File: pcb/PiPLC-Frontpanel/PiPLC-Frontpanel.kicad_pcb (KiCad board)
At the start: 2 copper layers, 160 x 43 mm, 3 parts

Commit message: [Frontpanel] Beautify
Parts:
- added REF**: Drill_LED5mm, MeineBib:Drill_LED5mm, F.Cu at (173.2, 103.8)
- added REF**: Drill_LED5mm, MeineBib:Drill_LED5mm, F.Cu at (189.2, 70.8)
- added REF**: Drill_LED5mm, MeineBib:Drill_LED5mm, F.Cu at (197.2, 103.8)
- added REF**: Drill_LED5mm, MeineBib:Drill_LED5mm, F.Cu at (189.2, 103.8)
- added REF**: Drill_LED5mm, MeineBib:Drill_LED5mm, F.Cu at (165.2, 70.8)
- added REF**: Drill_LED5mm, MeineBib:Drill_LED5mm, F.Cu at (157.2, 70.8)
- added REF**: Drill_LED5mm, MeineBib:Drill_LED5mm, F.Cu at (205.2, 103.8)
- added REF**: Drill_LED5mm, MeineBib:Drill_LED5mm, F.Cu at (132.6, 82.3)
- added REF**: Drill_LED5mm, MeineBib:Drill_LED5mm, F.Cu at (149.2, 70.8)
- added REF**: Drill_LED5mm, MeineBib:Drill_LED5mm, F.Cu at (181.2, 103.8)
- added REF**: Drill_LED5mm, MeineBib:Drill_LED5mm, F.Cu at (205.2, 70.8)
- added REF**: Drill_LED5mm, MeineBib:Drill_LED5mm, F.Cu at (149.2, 103.8)
- added REF**: Drill_LED5mm, MeineBib:Drill_LED5mm, F.Cu at (181.2, 70.8)
- added REF**: Drill_LED5mm, MeineBib:Drill_LED5mm, F.Cu at (173.2, 70.8)
- added REF**: Drill_LED5mm, MeineBib:Drill_LED5mm, F.Cu at (132.6, 92.3)
- added REF**: Drill_LED5mm, MeineBib:Drill_LED5mm, F.Cu at (157.2, 103.8)
- added REF**: Drill_LED5mm, MeineBib:Drill_LED5mm, F.Cu at (197.2, 70.8)
- added REF**: Drill_LED5mm, MeineBib:Drill_LED5mm, F.Cu at (165.2, 103.8)
- moved REF** 2.45 mm to (93.4, 94.5)
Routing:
- net (no net): track 0.00 -> 96.8 mm
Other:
- outline, holes or cut-outs redrawn
- board text added: "16A/250V AC | 16A/24V DC Relay outputs"
- board text added: "5-24V active HIGH Optocoupled inputs"

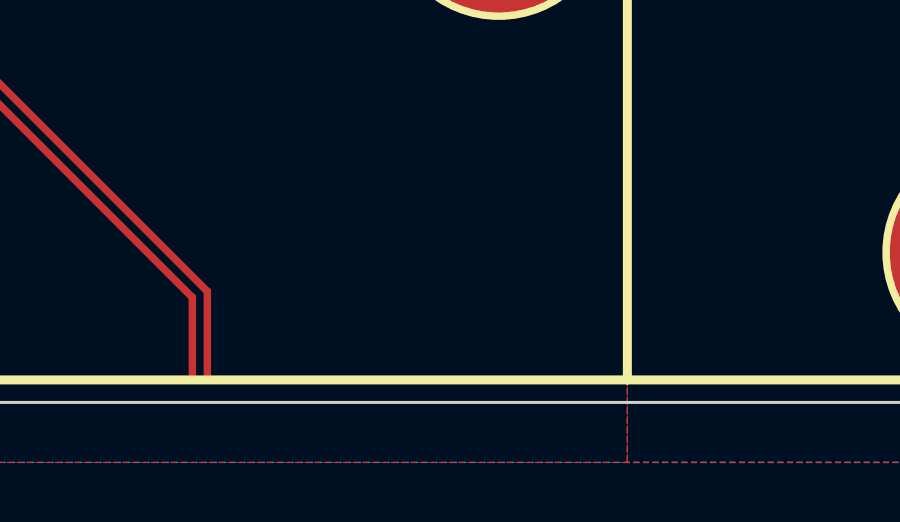
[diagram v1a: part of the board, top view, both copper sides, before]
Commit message: [HMI] Add JLC board number
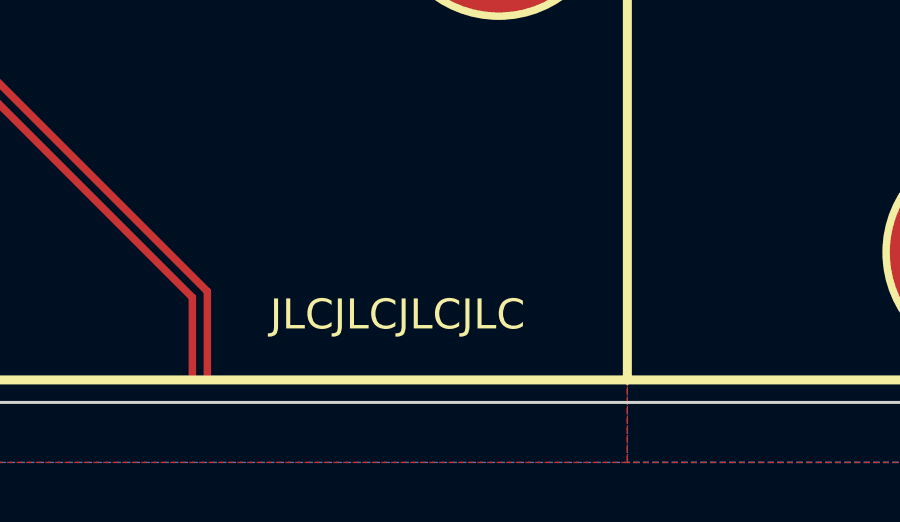
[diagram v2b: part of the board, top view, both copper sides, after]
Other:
- board text added: "JLCJLCJLCJLC"
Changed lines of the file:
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@@
     )
+  )
+  (gr_text "JLCJLCJLCJLC" (at 124.988 106.456) (layer "F.SilkS")
+    (effects (font (size 1 1) (thickness 0.15)) (justify left bottom))
   )
   (gr_text "Q5" (at 181.15 97.3) (layer "F.SilkS" knockout)
